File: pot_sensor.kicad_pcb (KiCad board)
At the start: 2 copper layers, 126 x 39 mm, 53 parts, among them J1 USB_C_Receptacle_USB2.0_14P, U1 ESP32-C3, U2 BQ24074RGT, U3 TPS63900, U4 W25Q32JVSS, U5 USBLC6-2P6, U7 HDC3020DEFR, U8 TPS22917DBV, Y1 ABM8-40MHZ

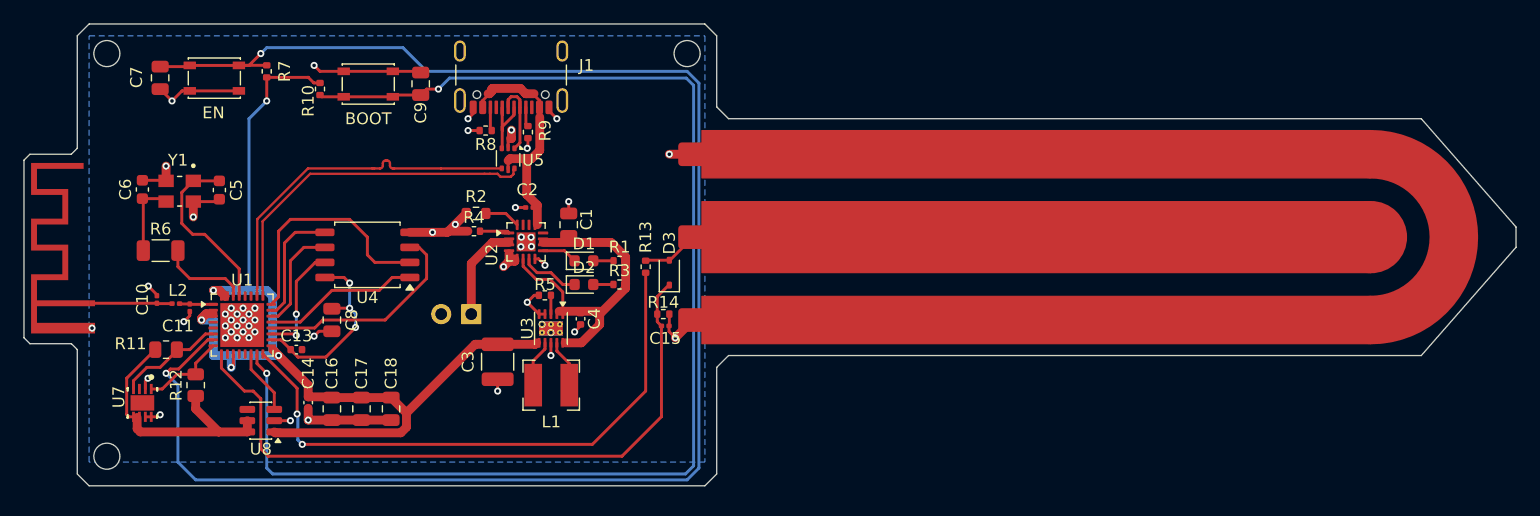
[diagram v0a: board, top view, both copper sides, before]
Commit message: Pending mfr/part number specification for fabrication
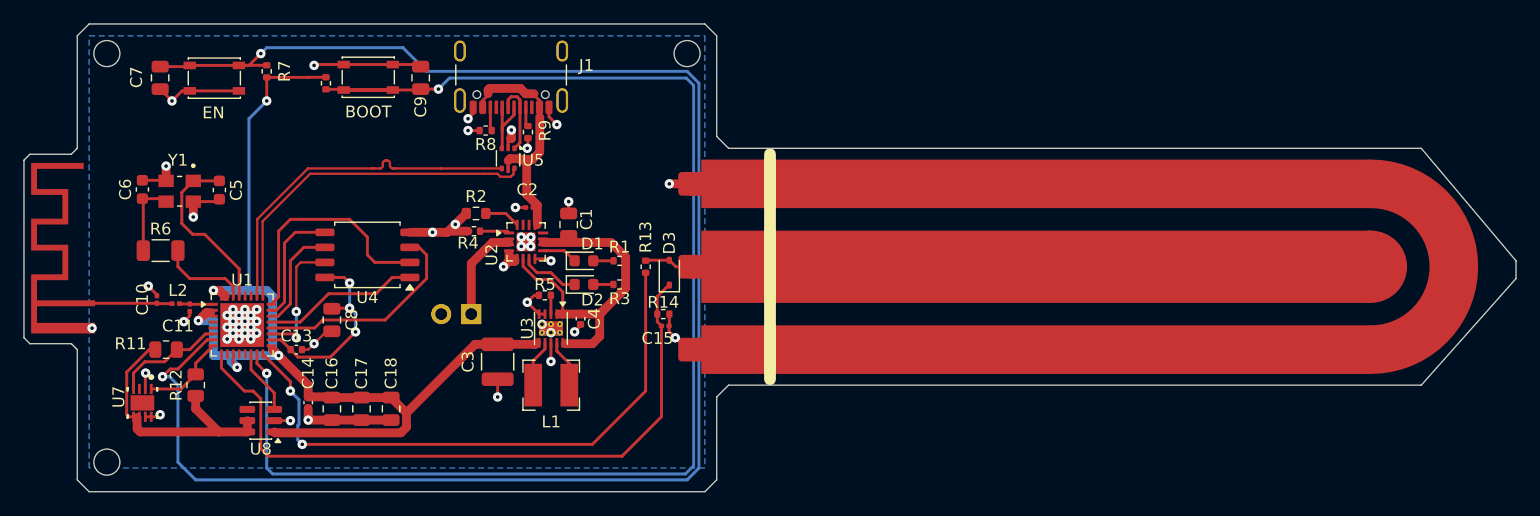
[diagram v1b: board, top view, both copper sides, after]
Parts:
- moved C12 2.50 mm to (109.2, 71.0)
- moved R10 0.69 mm to (78.5, 55.5)
- moved BOOT 0.58 mm to (82.1, 55.0)
- moved C9 0.50 mm to (86.5, 55.0)
- moved REF** 0.50 mm to (60.0, 87.5)
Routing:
- net /BOOT_PIN: track 111.2 -> 114.5 mm
- net GND: track 70.0 -> 72.6 mm
- net Net-(U1-SPIHD): track 9.82 -> 10.7 mm
- net Net-(U2-EN1): track 27.8 -> 28.7 mm
- net Net-(U1-CHIP_EN): track 140.4 -> 141.0 mm
- net Net-(U2-TS): track 3.11 -> 2.51 mm
- net Net-(C12-CIN): track 4.82 -> 4.29 mm
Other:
- board size 126 x 39 mm -> 126 x 39.5 mm

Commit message: Choosen references in mouser website
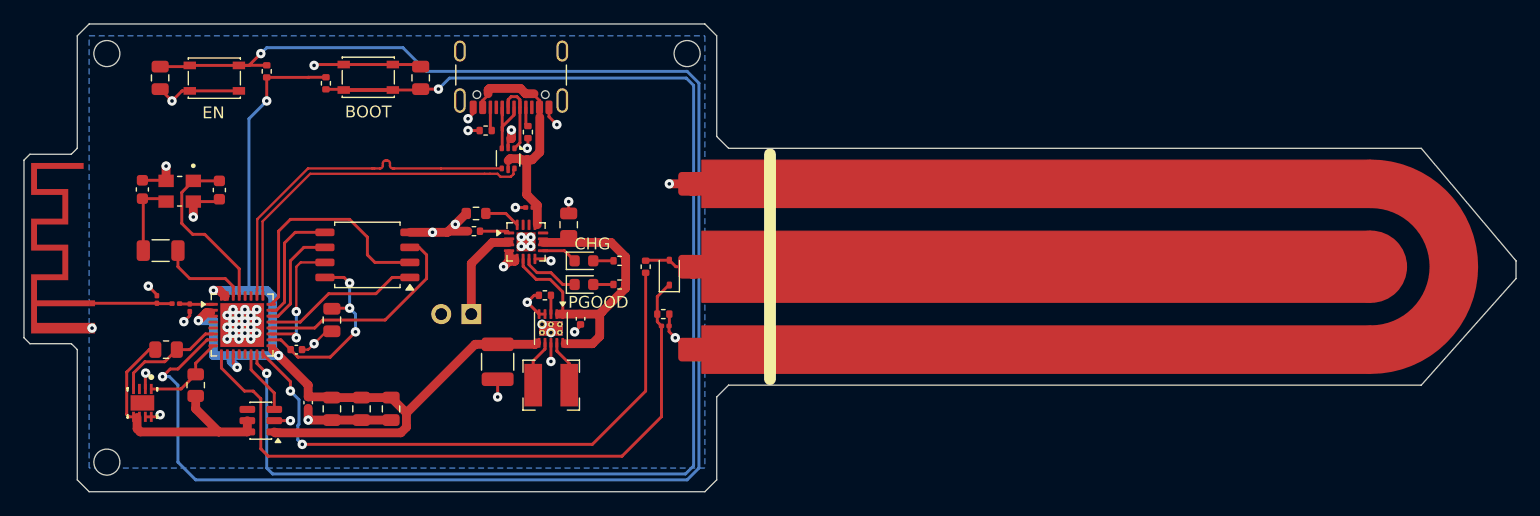
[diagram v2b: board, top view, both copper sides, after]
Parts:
- renumbered D1 to CHG, D2 to PGOOD

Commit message: Added zone fills for power distribution
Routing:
- net +3V3: track 89.0 -> 49.6 mm
- net VIN_USB: track 19.7 -> 0.00 mm
- added copper zone on F.Cu, net +3V3
- added copper zone on F.Cu, net VIN_USB

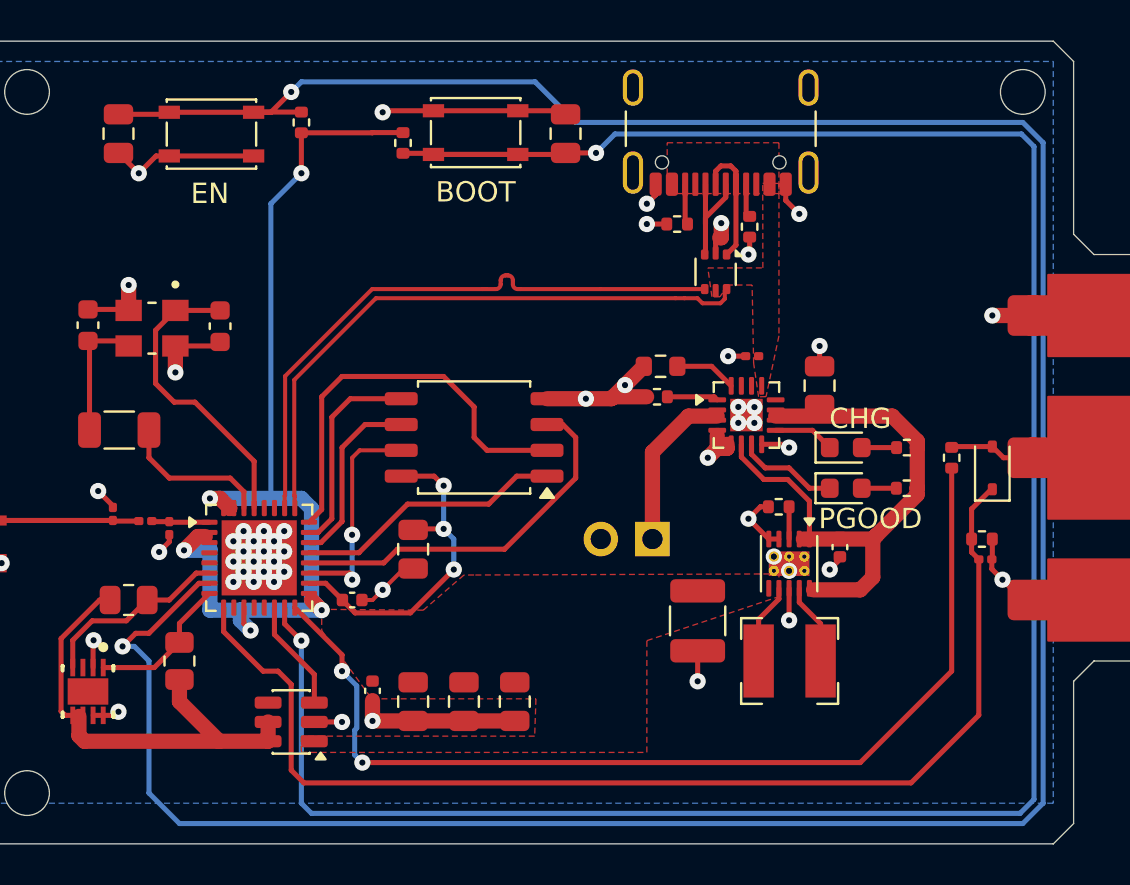
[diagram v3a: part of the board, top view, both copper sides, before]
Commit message: Updated powre distribution zones and added status LED
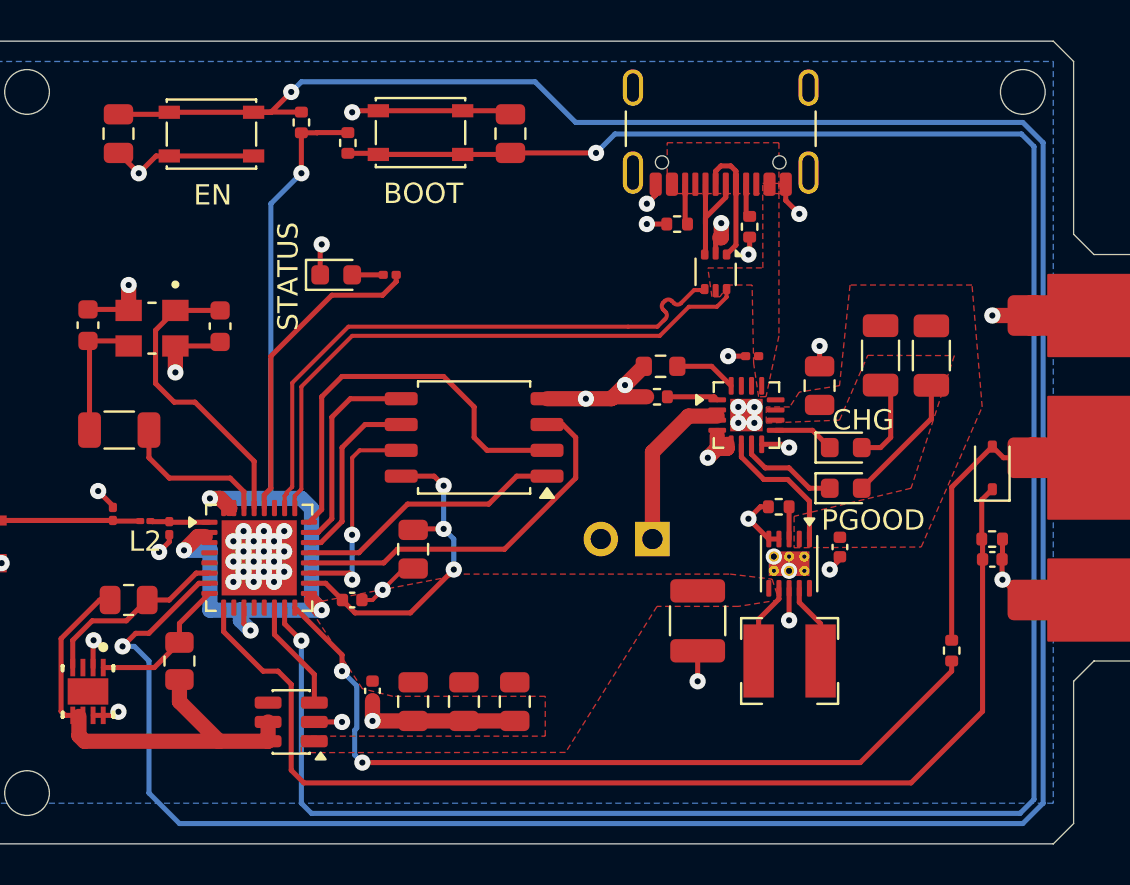
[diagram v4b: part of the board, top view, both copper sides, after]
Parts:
- added D4: GREEN, LED_SMD:LED_0603_1608Metric, F.Cu at (75.2, 62.0)
- added R15: 60, Resistor_SMD:R_0201_0603Metric, F.Cu at (77.8, 62.0)
- C15: footprint Capacitor_SMD:C_0201_0603Metric -> Capacitor_SMD:C_0402_1005Metric
- L2: footprint Inductor_SMD:L_0201_0603Metric -> Inductor_SMD:L_01005_0402Metric
- R1, R3: footprint Resistor_SMD:R_0402_1005Metric -> Resistor_SMD:R_1206_3216Metric
- moved R13 9.49 mm to (105.5, 80.5)
- moved R3 6.64 mm to (104.5, 66.0), turned to 90 degrees
- moved R1 4.72 mm to (102.0, 66.0), turned to 90 degrees
- moved C9 2.71 mm to (83.8, 55.0)
- moved R10 2.71 mm to (75.8, 55.5)
- moved SW2 2.71 mm to (79.4, 55.0)
- moved R14 0.50 mm to (107.5, 75.0)
- moved C15 0.34 mm to (107.5, 76.0)
- renumbered CHG to D1, PGOOD to D2, EN to SW1, BOOT to SW2
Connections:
- U1 pad 28: unconnected-(U1-U0TXD-Pad28) -> Net-(U1-U0TXD)
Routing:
- net Net-(U2-EN1): track 28.7 -> 6.74 mm
- net Net-(U1-U0TXD): track 0.00 -> 15.6 mm
- net /1MHz_PWM: track 49.7 -> 40.2 mm
- net Net-(C12-CIN): track 4.29 -> 12.6 mm
- net Net-(D2-A): track 1.70 -> 6.48 mm
- net /BOOT_PIN: track 114.5 -> 117.2 mm
- net +3V3: track 49.6 -> 46.9 mm
- net Net-(D1-A): track 1.71 -> 4.21 mm
- net Net-(D4-A): track 0.00 -> 1.53 mm
- net /USB_D-: track 29.9 -> 29.4 mm
- net GND: track 72.6 -> 72.7 mm, vias 53 -> 54
- added copper zone on F.Cu, net Net-(U2-EN1)
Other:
- board text added: "BOOT"
- board text added: "CHG"
- board text added: "EN"
- board text added: "PGOOD"
- board text added: "STATUS"

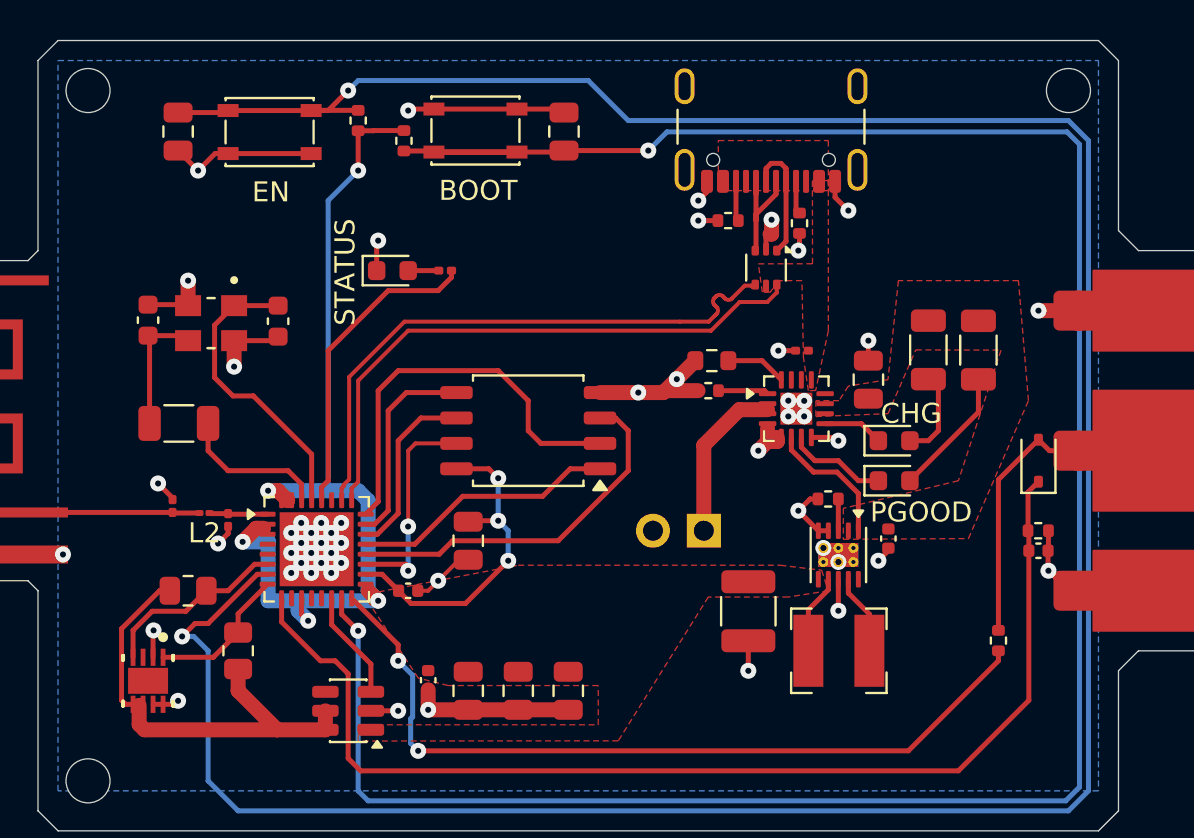
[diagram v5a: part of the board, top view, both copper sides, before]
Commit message: Updated schematic due to component changes
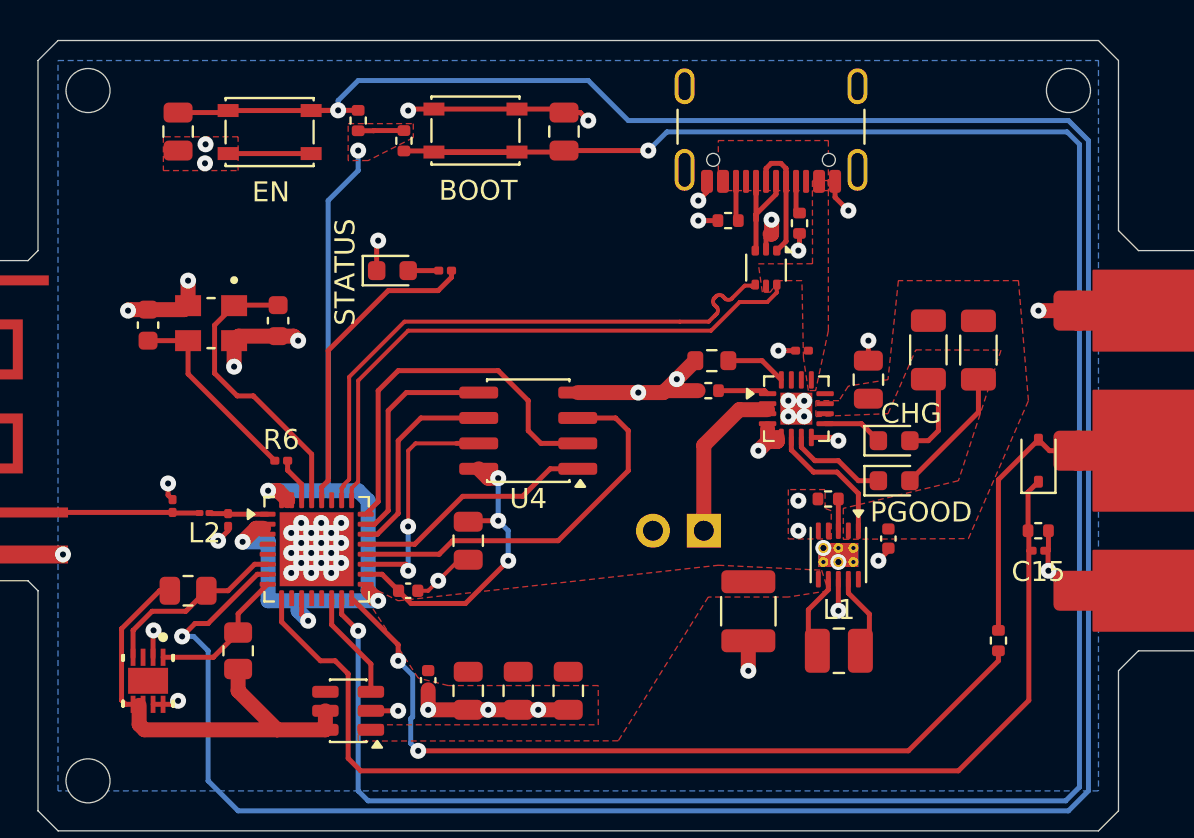
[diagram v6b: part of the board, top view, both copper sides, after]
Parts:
- C15: footprint Capacitor_SMD:C_0402_1005Metric -> Capacitor_SMD:C_0201_0603Metric
- C2: value 1µ -> 1u
- L1: footprint Inductor_SMD:L_Bourns-SRN4018 -> Inductor_SMD:L_1008_2520Metric
- R15: value 60 -> 60R
- R6: footprint Resistor_SMD:R_1206_3216Metric -> Resistor_SMD:R_0201_0603Metric
- U4: value W25Q32JVSS -> W25Q80DVSNIG; footprint Package_SO:SOIC-8_5.3x5.3mm_P1.27mm -> Package_SO:SOIC-8_3.9x4.9mm_P1.27mm
- moved R6 5.45 mm to (69.7, 71.5)
- moved C6 0.25 mm to (63.0, 64.7)
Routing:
- net Net-(U1-XTAL_P): track 7.53 -> 2.26 mm
- net Net-(C6-Pad1): track 6.52 -> 10.1 mm
- net GND: track 72.7 -> 70.8 mm, vias 54 -> 61
- net Net-(U1-SPIWP): track 18.5 -> 19.6 mm
- net Net-(U1-SPIQ): track 20.3 -> 19.2 mm
- net Net-(U1-SPIHD): track 10.7 -> 11.9 mm
- net Net-(U1-SPID): track 10.2 -> 11.3 mm
- net Net-(U1-SPICS0): track 13.3 -> 12.2 mm
- net Net-(U1-SPICLK): track 9.07 -> 10.2 mm
- net +3V3: track 46.9 -> 45.9 mm
- added copper zone on F.Cu, net GND

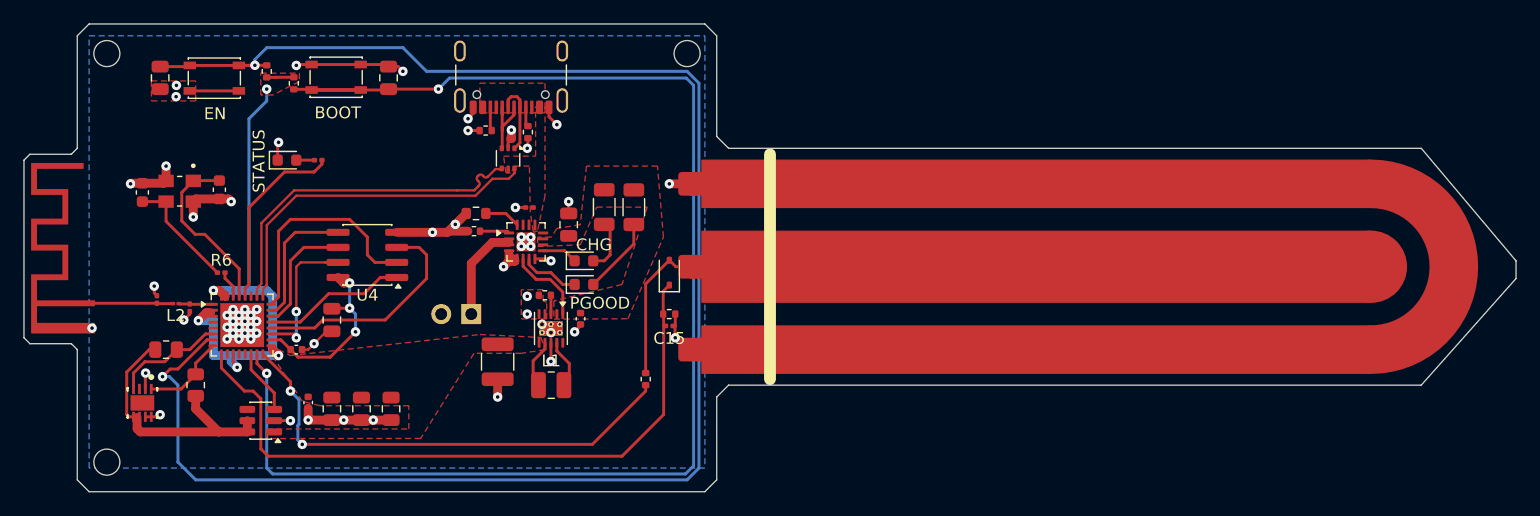
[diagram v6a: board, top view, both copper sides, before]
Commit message: Added signal layer ground pour and added design rule exceptions to clear up error messages
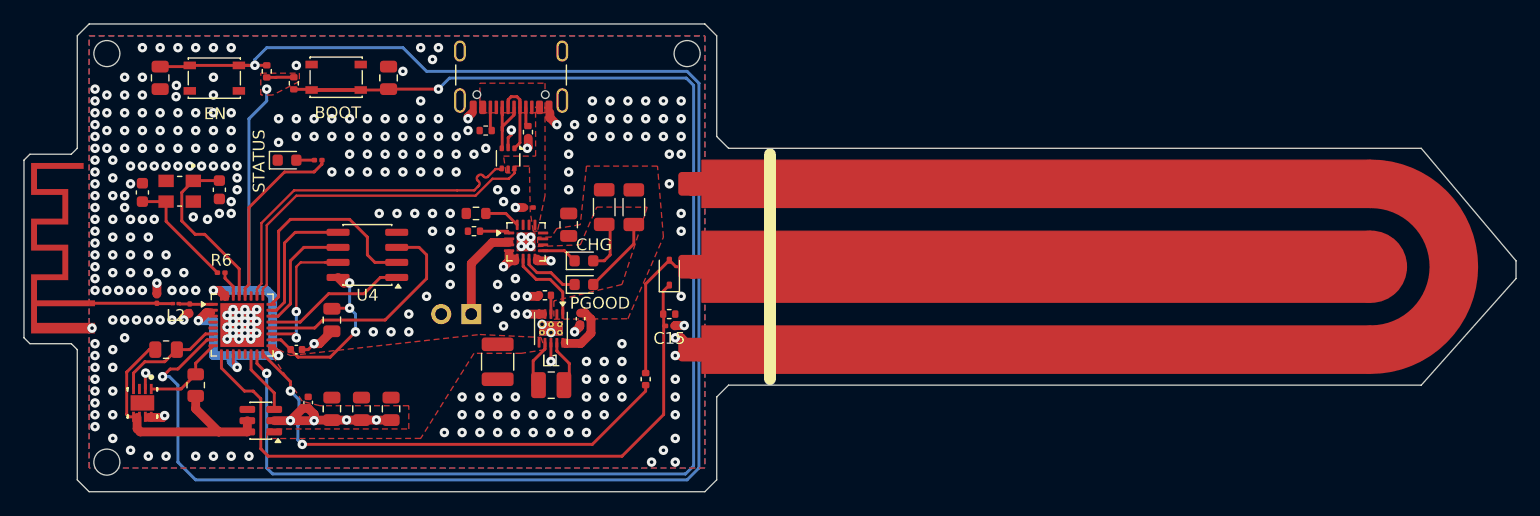
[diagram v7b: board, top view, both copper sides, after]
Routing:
- net GND: track 70.8 -> 38.9 mm, vias 61 -> 315
- net Net-(U2-EN1): track 6.74 -> 11.6 mm

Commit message: Pending another part re-selection
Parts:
- C10, C11, C15, C2: footprint Capacitor_SMD:C_0201_0603Metric -> Capacitor_SMD:C_0402_1005Metric
- L2: footprint Inductor_SMD:L_01005_0402Metric -> Inductor_SMD:L_0402_1005Metric
- R15: footprint Resistor_SMD:R_0201_0603Metric -> Resistor_SMD:R_0603_1608Metric
- R6: footprint Resistor_SMD:R_0201_0603Metric -> Resistor_SMD:R_0402_1005Metric
- moved L2 0.80 mm to (65.0, 74.1)
- moved C10 0.74 mm to (63.5, 73.6)
- moved R15 0.66 mm to (78.5, 62.0)
- moved C11 0.52 mm to (66.5, 74.6)
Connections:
- JSTconnector1 pad 1: Net-(JSTconnector1-Pad+) -> (no net)
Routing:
- net GND: track 38.9 -> 46.2 mm, vias 315 -> 319
- net Net-(U3-LX1): track 4.01 -> 6.82 mm
- net Net-(U3-LX2): track 3.99 -> 6.74 mm
- net Net-(A1-Feed): track 6.76 -> 5.79 mm
- net Net-(U1-U0TXD): track 15.6 -> 16.6 mm
- net Net-(U1-LNA_IN): track 2.91 -> 3.50 mm
